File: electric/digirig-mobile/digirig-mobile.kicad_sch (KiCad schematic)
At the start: 67 parts, among them J1 USB, J2 PJ-320A, J3 PJ-320A, Q1 MMBT5551L, Q2 MMBT5551L, U1 CP2102N-A02-GQFN24, U2 USB2412-DZK-TR, U3 ADM3101E, U4 CM108, Y1 24MHz, Y2 12MHz

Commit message: Digirig Mobile 1.9 - final
final cosmetic touches on digirig mobile 1.9
folders structure reorganization
logo resources mods
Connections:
- net at D1.2 (A): now also JP1.1 (A); no longer JP1.3 (C)
- net at U3.2 (R_OUT): now also JP1.3 (C); no longer JP1.1 (A)
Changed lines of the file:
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@@
     (effects (font (size 1.27 1.27)) (justify left bottom))
   )
-  (text "USB Hub" (at 26.67 26.67 0)
+  (text "USB Hub" (at 25.4 25.4 0)
     (effects (font (size 1.27 1.27)) (justify left bottom))
   )
@@
     (pin "1")
   )
-  (symbol (lib_id "digirig:SolderJumper_9") (at 118.11 217.17 270) (mirror x) (unit 1)
+  (symbol (lib_id "digirig:SolderJumper_9") (at 118.11 217.17 270) (unit 1)
     (in_bom no) (on_board yes)
-    (property "Reference" "JP1" (id 0) (at 110.49 219.71 90)
-      (effects (font (size 1.27 1.27)) (justify left))
-    )
-    (property "Value" "RS232" (id 1) (at 109.22 222.25 90)
-      (effects (font (size 1.27 1.27)) (justify left))
-    )
-    (property "Footprint" "footprints:SolderJumper9-BCu" (id 2) (at 124.46 218.44 0)
-      (effects (font (size 1.27 1.27)) hide)
-    )
+    (property "Reference" "JP1" (id 0) (at 110.49 214.63 90)
+      (effects (font (size 1.27 1.27)) (justify left))
+    )
+    (property "Value" "RS232" (id 1) (at 109.22 212.09 90)
+      (effects (font (size 1.27 1.27)) (justify left))
+    )
+    (property "Footprint" "footprints:SolderJumper9-BCu" (id 2) (at 124.46 215.9 0)
+      (effects (font (size 1.27 1.27)) hide)
+    )

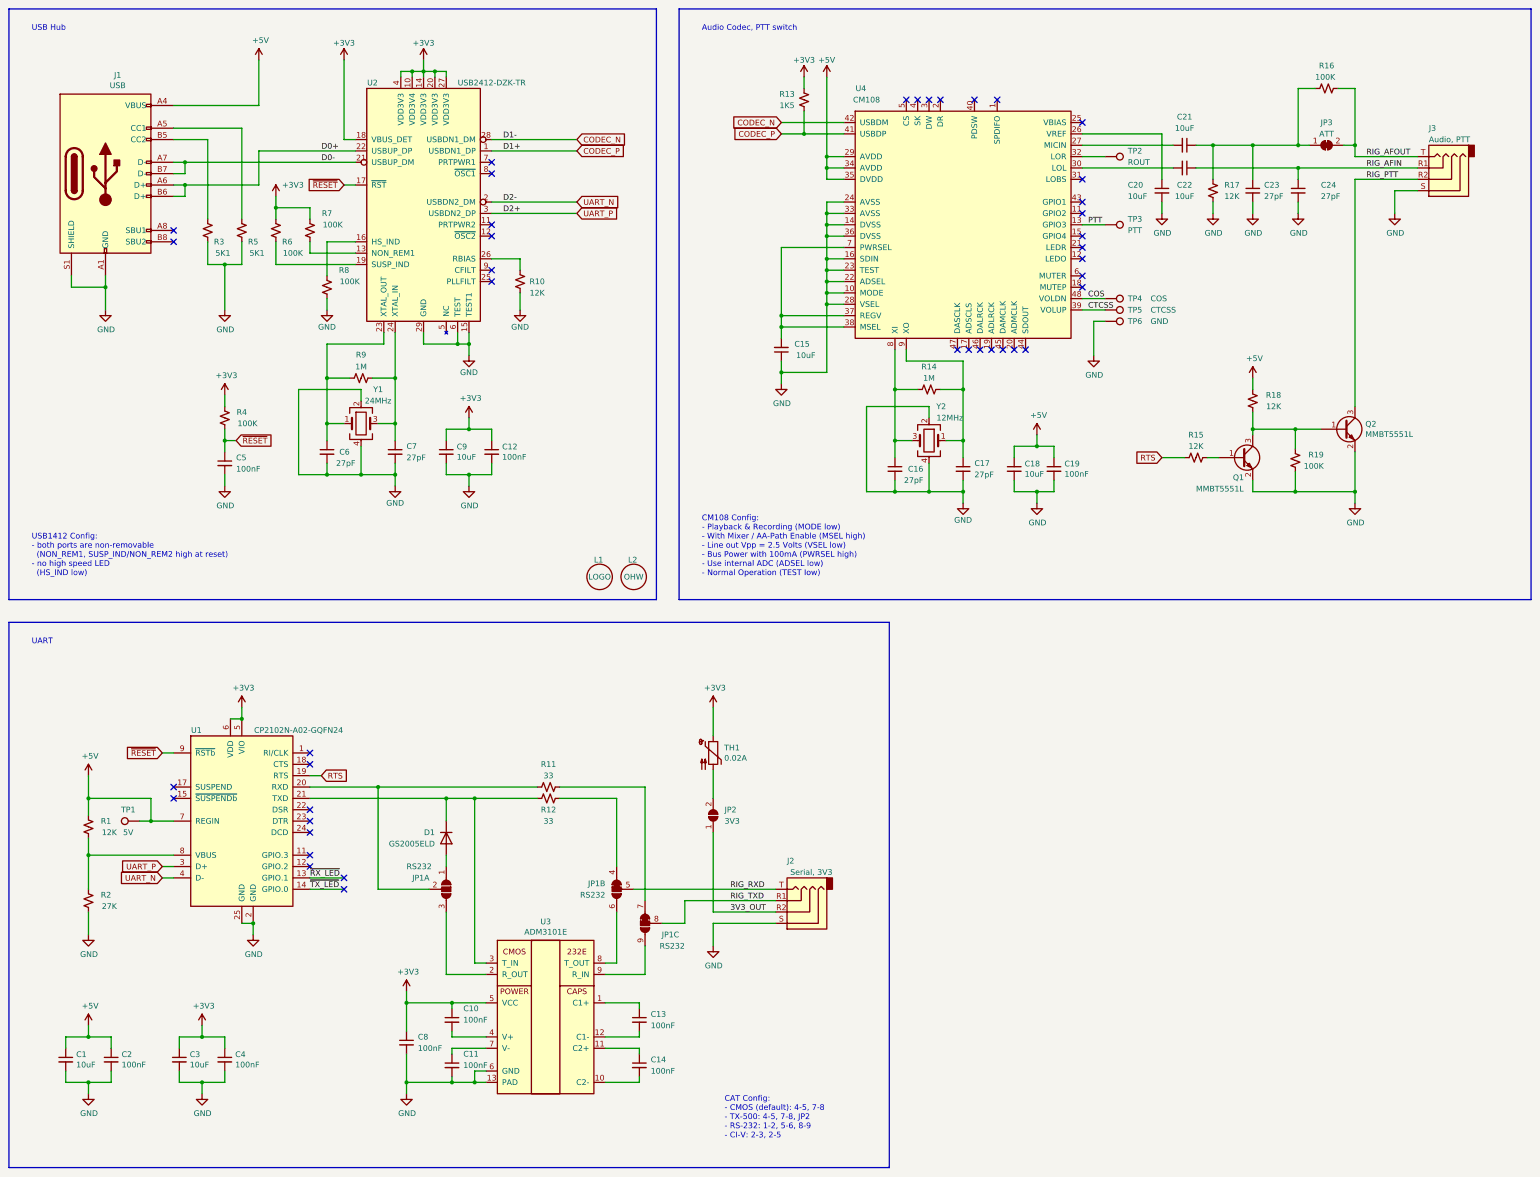
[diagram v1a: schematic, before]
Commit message: Digirig Mobile Rev 1.11
Electrical for Digirig Mobile Rev 1.11
- move from end of life CM108AH to current CM108B
- move to a smaller enclosure
- small adjustments to filtering
- KiCad version update
Resource file updates
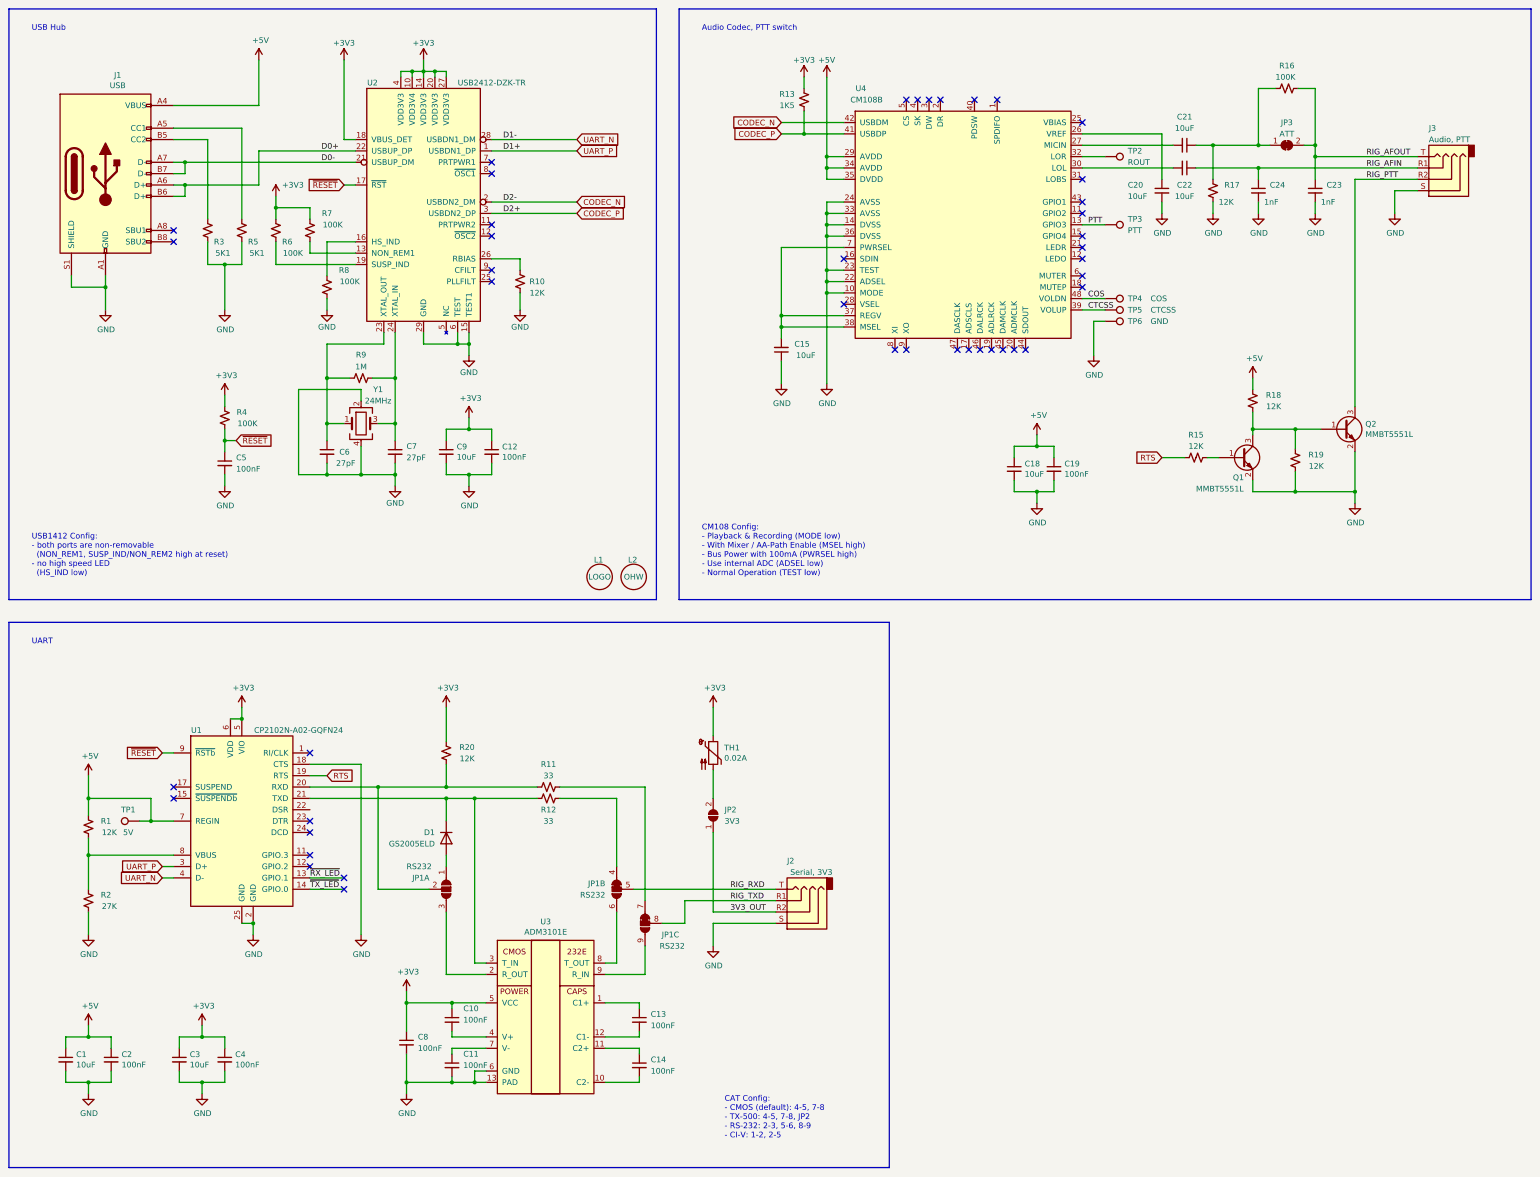
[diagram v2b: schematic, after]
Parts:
- removed C16, C17: 27pF, Capacitor_SMD:C_0402_1005Metric, symbol Device:C_Small
- removed R14: 1M, Resistor_SMD:R_0402_1005Metric, symbol Device:R_Small_US
- removed Y2: 12MHz, Crystal:Crystal_SMD_3225-4Pin_3.2x2.5mm, symbol Device:Crystal_GND24
- added R20: 12K, Resistor_SMD:R_0402_1005Metric, symbol Device:R_Small_US
- C1, C15, C18, C20, C21, C22, C3, C9: LCSC (none) -> C15525
- C10, C11, C12, C13, C14, C19, C2, C4, C5, C8: LCSC (none) -> C1525
- C23, C24: value 27pF -> 1nF; LCSC (none) -> C1523
- C6, C7: LCSC (none) -> C1557
- D1: LCSC (none) -> C18716421
- J1: footprint footprints:USB_C_Receptacle_HRO_TYPE-C-31-M-12 -> Connector_USB:USB_C_Receptacle_HRO_TYPE-C-31-M-12; LCSC (none) -> C393939
- J2: value PJ-320A -> PJ-320A-GREEN; footprint footprints:TRRS-PJ-320A -> footprints:Jack_3.5mm_PJ320D_Horizontal; LCSC (none) -> C9900076584
- J3: footprint footprints:TRRS-PJ-320A -> footprints:Jack_3.5mm_PJ320D_Horizontal; LCSC (none) -> C431535
- Q1, Q2: footprint Package_TO_SOT_SMD:SOT-23 -> footprints:SOT-23; LCSC (none) -> C152516
- R1, R10, R15, R17, R18: LCSC (none) -> C25752
- R11, R12: LCSC (none) -> C25105
- R13: LCSC (none) -> C25867
- R16, R4, R6, R7, R8: LCSC (none) -> C25741
- R19: value 100K -> 12K; LCSC (none) -> C25752
- R2: LCSC (none) -> C25771
- R3, R5: LCSC (none) -> C25905
- R9: LCSC (none) -> C26083
- TH1: LCSC (none) -> C1884486
- U1: LCSC (none) -> C1550551
- U2: LCSC (none) -> C622609
- U3: LCSC (none) -> C514336
- U4: value CM108 -> CM108B; LCSC (none) -> C371347
- Y1: footprint Crystal:Crystal_SMD_3225-4Pin_3.2x2.5mm -> Crystal:Crystal_SMD_2520-4Pin_2.5x2.0mm; LCSC (none) -> C70590
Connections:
- net +3V3: now also R20.2
- net CODEC_N: now also U2.2 (USBDN2_DM); no longer U2.28 (USBDN1_DM)
- net CODEC_P: now also U2.3 (USBDN2_DP); no longer U2.1 (USBDN1_DP)
- net GND: now also U1.18 (CTS); no longer U4.16 (SDIN), U4.28 (VSEL)
- net RIG_AFOUT: now also C23.1
- net UART_N: now also U2.28 (USBDN1_DM); no longer U2.2 (USBDN2_DM)
- net UART_P: now also U2.1 (USBDN1_DP); no longer U2.3 (USBDN2_DP)
- net at JP1.2 (B), R11.2, U1.20 (RXD): now also R20.1
- net at C21.1, JP3.1 (A), R16.2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: no longer C23.1
- no-connect marks 41 -> 43
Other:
- note added: "CAT Config: - CMOS (default): 4-5, 7-8 - TX-500: 4-5, 7-8, JP2 - RS-232: 2-3, 5-6, 8-9 - CI-V: 1-2, 2-5"
- note added: "CM108 Config: - Playback & Recording (MODE low) - With Mixer / AA-Path Enable (MSEL high) - Bus Power with 100mA (PWRSEL high) - Use internal ADC (ADSEL low) - Normal Operation (TEST low)"
- note removed: "CAT Config: - CMOS (default): 4-5, 7-8 - TX-500: 4-5, 7-8, JP2 - RS-232: 1-2, 5-6, 8-9 - CI-V: 2-3, 2-5"
- note removed: "CM108 Config: - Playback & Recording (MODE low) - With Mixer / AA-Path Enable (MSEL high) - Line out Vpp = 2.5 Volts (VSEL low) - Bus Power with 100mA (PWRSEL high) - Use internal ADC (ADSEL low) - Normal Operation (TEST low)"
- moved on the sheet: C23, C24, JP3, R16
